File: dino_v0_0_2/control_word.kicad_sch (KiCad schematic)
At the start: 6 parts, among them U28 74LS138, U29 74LS138, U30 74LS138

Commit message: feat(dino): complete v0.0.3 schematic — all 11 sheets netlist-clean
- wire MAR sheet: '373 LO/HI latches, 2x '245 M-bus drive, A15 decode
  (ROM_EN/~RAM_EN), LE stamps off /MAR_LO_LOAD//MAR_HI_LOAD
- fix PC_MAR_MUX polarity: PC '245s enabled on bit14=0, inverted vs
  bit-map convention (PC=1); add ~PC_MAR_MUX inverter, relabel U13/U14
- wire all 7 control-word bus taps [15:9] (SA0-2, END, PC_UP,
  PC_MAR_MUX, HALT) — label pairs had no wire between them
- untie NONE/NC '138 outputs: totem-pole bus fight on every microword;
  each unused output now individually no_connect
- build END (U61 NOR: ~MR = RESET|END, sync T-state clear) and HALT
  (T-state freeze via CET, clock keeps running)
- build COND/JNZ (U62: ~PC_LOAD = taken-JNZ | unconditional-JMP)
- claim src code 111 as /SW_OUT: IN port — DIP switches through 10k
  pull-ups onto W bus via '244; LED bank active-high off OB0-7
- add U66 missing power unit + decouplers (C63-C66)
- tools: kicad_gen_sheet.py (declarative YAML/JSON sheet generator,
  deterministic uuid5, collision-checked), kicad_xsheet_audit.py
  (cross-sheet contract audit); archive stale testing-strategy doc
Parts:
- added C66: 0.1µF, symbol Device:C_Small
- added U62: 74LS02, symbol 74xx:74LS02
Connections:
- net +5V: now also C66.1, U62.14 (VCC)
- net GND: now also C66.2, U62.11, U62.12, U62.7 (GND)
- net ~{COND}: now also U62.2
- net ~{PC_LOAD}: now also U62.10; no longer U29.13 (O2)
- removed net NC: U28.7 (O7), U29.10 (O5), U29.7 (O7)
- removed net NONE: U28.15 (O0), U29.15 (O0), U30.15 (O0)
- new net COND_TAKEN: U62.1, U62.8
- new net FLAG_Z: U62.3
- new net PC_LOAD_JMP: U62.4, U62.9
- new net ~{PC_LOAD_JMP}: U29.13 (O2), U62.5, U62.6
- new net ~{SW_OUT}: U28.7 (O7)
- no-connect marks 0 -> 6

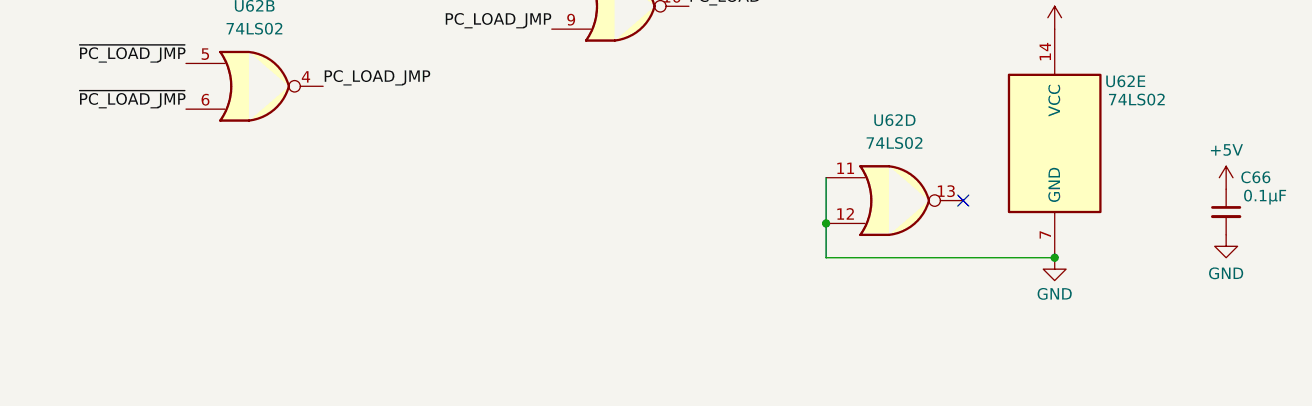
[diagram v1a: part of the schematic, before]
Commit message: feat(dino): generate + stamp per-sheet I/O contracts
Each module's boundary signals (IN/OUT/BIDIR with counterpart sheets)
derived from the kicad-cli netlist and placed as a text block on the
physical sheet, so a bench rig knows exactly what to drive and observe
per board. kicad_contracts.py regenerates both the markdown and the
stamps idempotently; stamping verified electrically neutral.
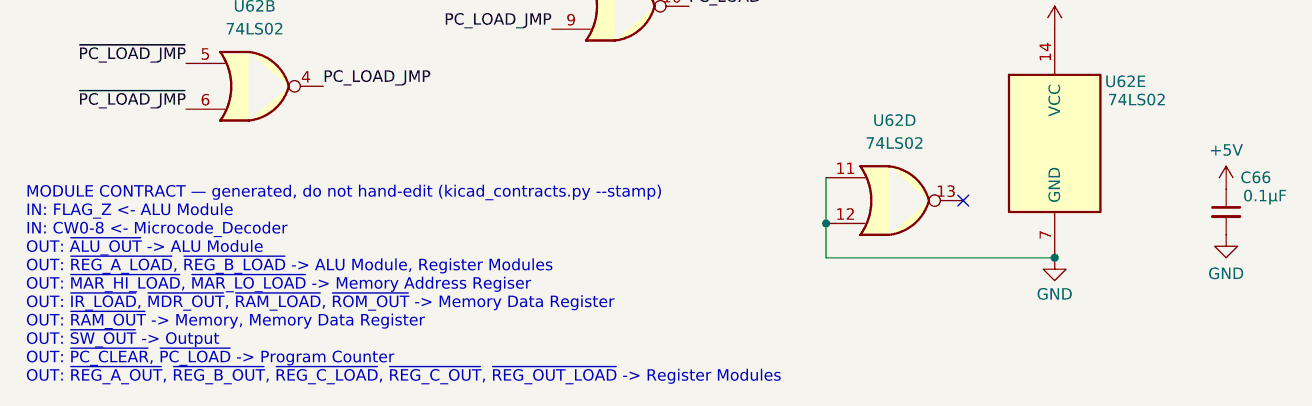
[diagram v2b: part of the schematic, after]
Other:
- note added: "MODULE CONTRACT — generated, do not hand-edit (kicad_contracts.py --stamp) IN: FLAG_Z <- ALU Module IN: CW0-8 <- Microcode_Decoder OUT: ~{ALU_OUT} -> ALU Module OUT: ~{REG_A_LOAD}, ~{REG_B_LOAD} -> ALU Module, Register Modules OUT: ~{MAR_HI_LOAD}, ~{MAR_LO_LOAD} -> Memory Address Regiser OUT: ~{IR_LOAD}, ~{MDR_OUT}, ~{RAM_LOAD}, ~{ROM_OUT} -> Memory Data Register OUT: ~{RAM_OUT} -> Memory, Memory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"
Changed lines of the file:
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@@
+		)
+	)
+	(text "MODULE CONTRACT — generated, do not hand-edit (kicad_contracts.py --stamp)\nIN: FLAG_Z <- ALU Module\nIN: CW0-8 <- Microcode_Decoder\nOUT: ~{ALU_OUT} -> ALU Module\nOUT: ~{REG_A_LOAD}, ~{REG_B_LOAD} -> ALU Module, Register Modules\nOUT: ~{MAR_HI_LOAD}, ~{MAR_LO_LOAD} -> Memory Address Regiser\nOUT: ~{IR_LOAD}, ~{MDR_OUT}, ~{RAM_LOAD}, ~{ROM_OUT} -> Memory Data Register\nOUT: ~{RAM_OUT} -> Memory, Memory Data Register\nOUT: ~{SW_OUT} -> Output\nOUT: ~{PC_CLEAR}, ~{PC_LOAD} -> Program Counter\nOUT: ~{REG_A_OUT}, ~{REG_B_OUT}, ~{REG_C_LOAD}, ~{REG_C_OUT}, ~{REG_OUT_LOAD} -> Register Modules"
+		(exclude_from_sim no)
+		(at 15.24 210.91 0)
+		(effects
+			(font
+				(size 1.27 1.27)
+			)
+			(justify left bottom)
 		)
 	)

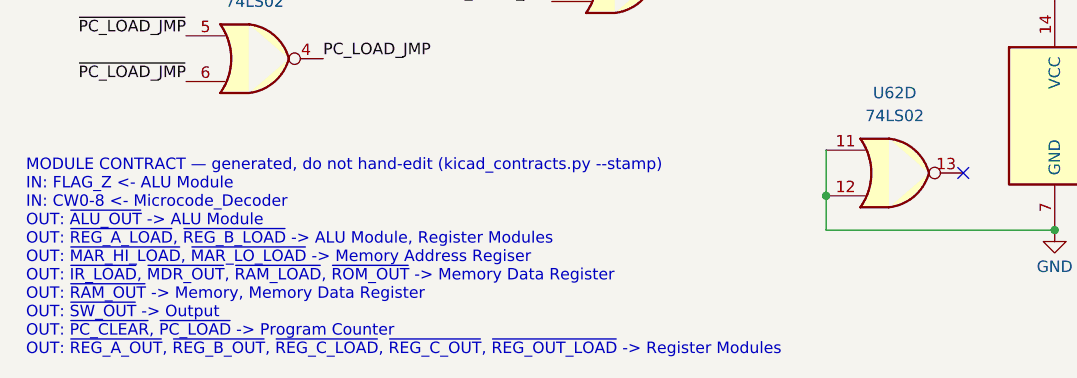
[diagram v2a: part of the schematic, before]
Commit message: fix(dino): three review-found schematic bugs on microcode/memory
- microcode U9/U15: ~WE tied +5V, A12 tied GND (were floating with NC
  flags — in-circuit corruption + image-aliasing hazard on AT28C64B)
- memory: label the U24.~OE/U19.CE net ~{ROM_OUT} — the ROM read path
  had no driver as drawn (caught by new kicad_netlist.py --lint)
- memory: U21 (RAM-side '245) CE now AND(~RAM_OUT, ~WRITE_DIR) via U51
  spare gates — was enabled by ~RAM_EN alone, buffering floating RAM DQ
  onto MDR against register drivers whenever MAR parked on a RAM
  address with no RAM op in flight

Contracts restamped; all verified in kicad_netlist.py + kicad-cli
export; lint clean project-wide.
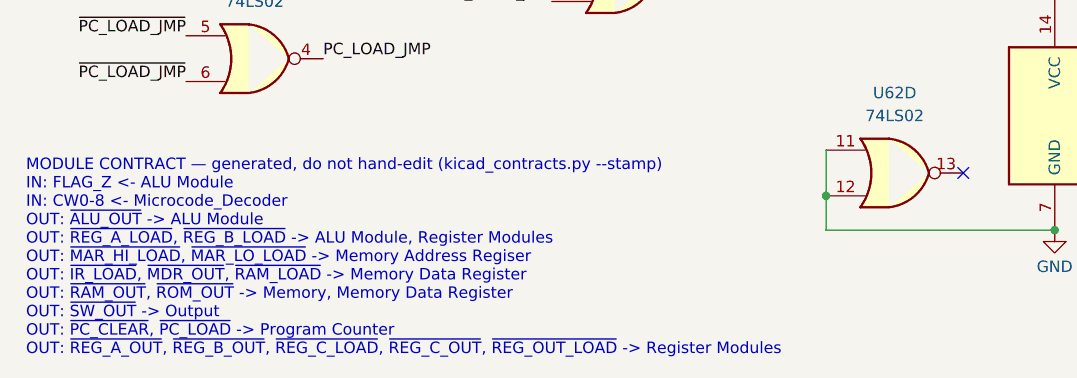
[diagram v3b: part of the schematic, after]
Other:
- note added: "MODULE CONTRACT — generated, do not hand-edit (kicad_contracts.py --stamp) IN: FLAG_Z <- ALU Module IN: CW0-8 <- Microcode_Decoder OUT: ~{ALU_OUT} -> ALU Module OUT: ~{REG_A_LOAD}, ~{REG_B_LOAD} -> ALU Module, Register Modules OUT: ~{MAR_HI_LOAD}, ~{MAR_LO_LOAD} -> Memory Address Regiser OUT: ~{IR_LOAD}, ~{MDR_OUT}, ~{RAM_LOAD} -> Memory Data Register OUT: ~{RAM_OUT}, ~{ROM_OUT} -> Memory, Memory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"
- note removed: "MODULE CONTRACT — generated, do not hand-edit (kicad_contracts.py --stamp) IN: FLAG_Z <- ALU Module IN: CW0-8 <- Microcode_Decoder OUT: ~{ALU_OUT} -> ALU Module OUT: ~{REG_A_LOAD}, ~{REG_B_LOAD} -> ALU Module, Register Modules OUT: ~{MAR_HI_LOAD}, ~{MAR_LO_LOAD} -> Memory Address Regiser OUT: ~{IR_LOAD}, ~{MDR_OUT}, ~{RAM_LOAD}, ~{ROM_OUT} -> Memory Data Register OUT: ~{RAM_OUT} -> Memory, Memory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"
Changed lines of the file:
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@@
 		)
 	)
-	(text "MODULE CONTRACT — generated, do not hand-edit (kicad_contracts.py --stamp)\nIN: FLAG_Z <- ALU Module\nIN: CW0-8 <- Microcode_Decoder\nOUT: ~{ALU_OUT} -> ALU Module\nOUT: ~{REG_A_LOAD}, ~{REG_B_LOAD} -> ALU Module, Register Modules\nOUT: ~{MAR_HI_LOAD}, ~{MAR_LO_LOAD} -> Memory Address Regiser\nOUT: ~{IR_LOAD}, ~{MDR_OUT}, ~{RAM_LOAD}, ~{ROM_OUT} -> Memory Data Register\nOUT: ~{RAM_OUT} -> Memory, Memory Data Register\nOUT: ~{SW_OUT} -> Output\nOUT: ~{PC_CLEAR}, ~{PC_LOAD} -> Program Counter\nOUT: ~{REG_A_OUT}, ~{REG_B_OUT}, ~{REG_C_LOAD}, ~{REG_C_OUT}, ~{REG_OUT_LOAD} -> Register Modules"
+	(text "MODULE CONTRACT — generated, do not hand-edit (kicad_contracts.py --stamp)\nIN: FLAG_Z <- ALU Module\nIN: CW0-8 <- Microcode_Decoder\nOUT: ~{ALU_OUT} -> ALU Module\nOUT: ~{REG_A_LOAD}, ~{REG_B_LOAD} -> ALU Module, Register Modules\nOUT: ~{MAR_HI_LOAD}, ~{MAR_LO_LOAD} -> Memory Address Regiser\nOUT: ~{IR_LOAD}, ~{MDR_OUT}, ~{RAM_LOAD} -> Memory Data Register\nOUT: ~{RAM_OUT}, ~{ROM_OUT} -> Memory, Memory Data Register\nOUT: ~{SW_OUT} -> Output\nOUT: ~{PC_CLEAR}, ~{PC_LOAD} -> Program Counter\nOUT: ~{REG_A_OUT}, ~{REG_B_OUT}, ~{REG_C_LOAD}, ~{REG_C_OUT}, ~{REG_OUT_LOAD} -> Register Modules"
 		(exclude_from_sim no)
 		(at 15.24 210.91 0)
